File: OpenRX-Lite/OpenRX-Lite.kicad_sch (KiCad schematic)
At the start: 0 parts

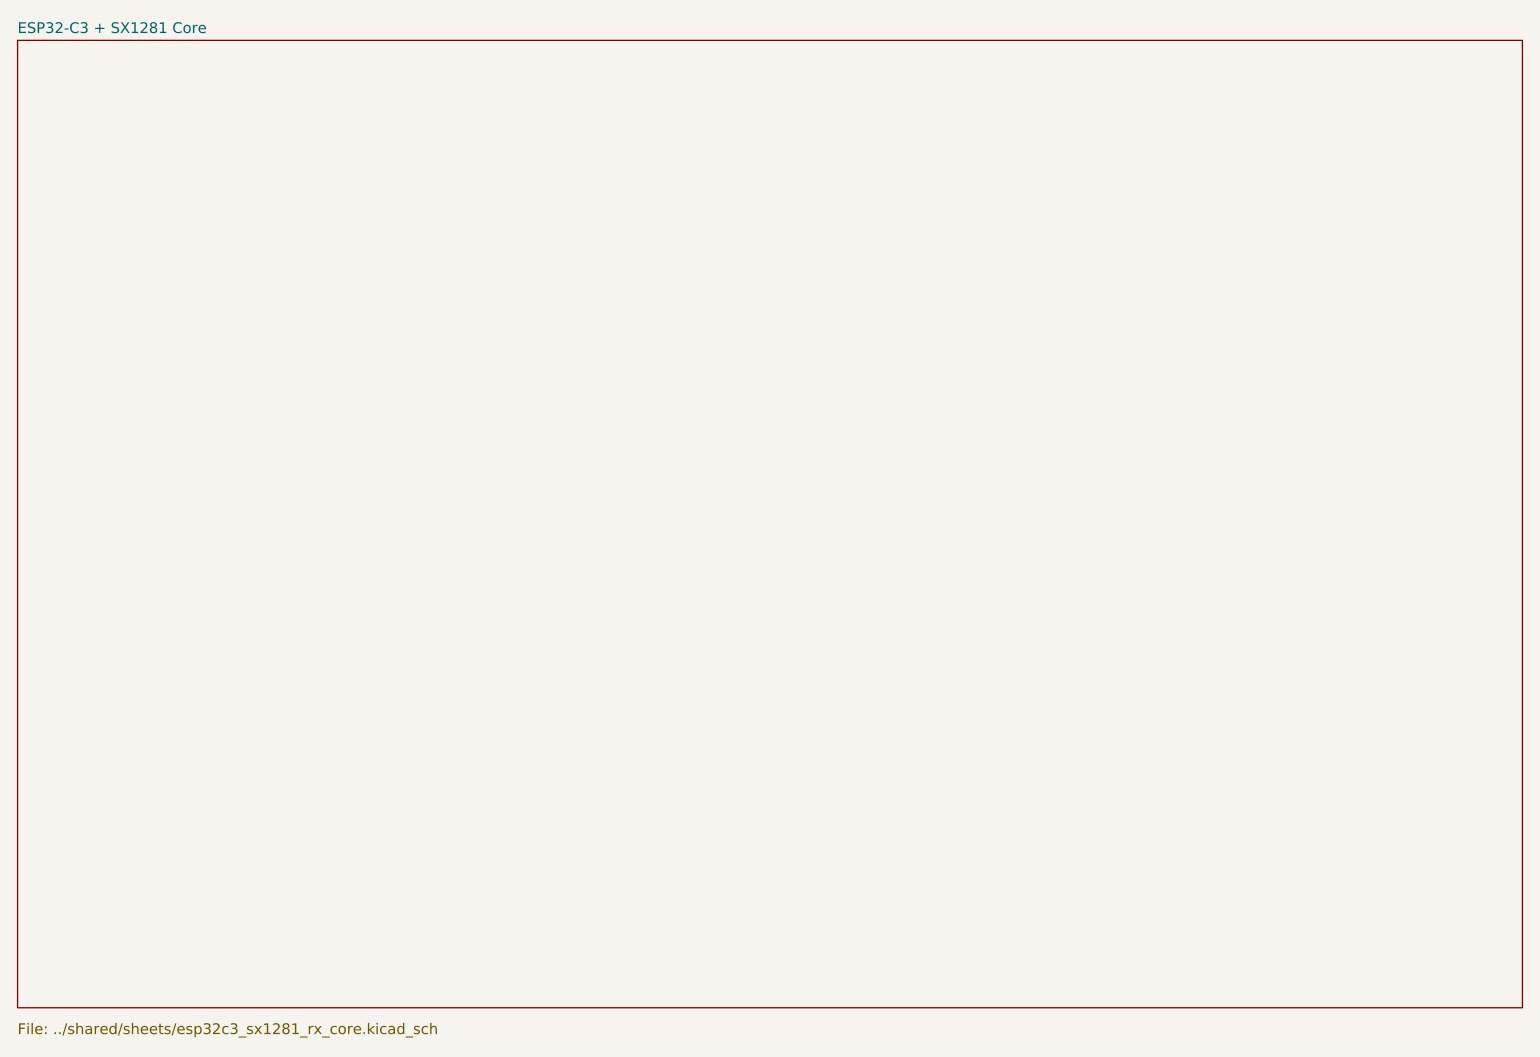
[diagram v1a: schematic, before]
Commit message: Unify library tables, import RFX2401C, Lite schematic capture
- All 6 projects now share OpenRX-Shared + OpenRX-Lite lib tables
- Import RFX2401C (C19213) into shared library with 3D model path fix
- OpenRX-Lite schematic: 0 ERC errors (captured in KiCad GUI)
- Add .gitignore for .lck and .history files
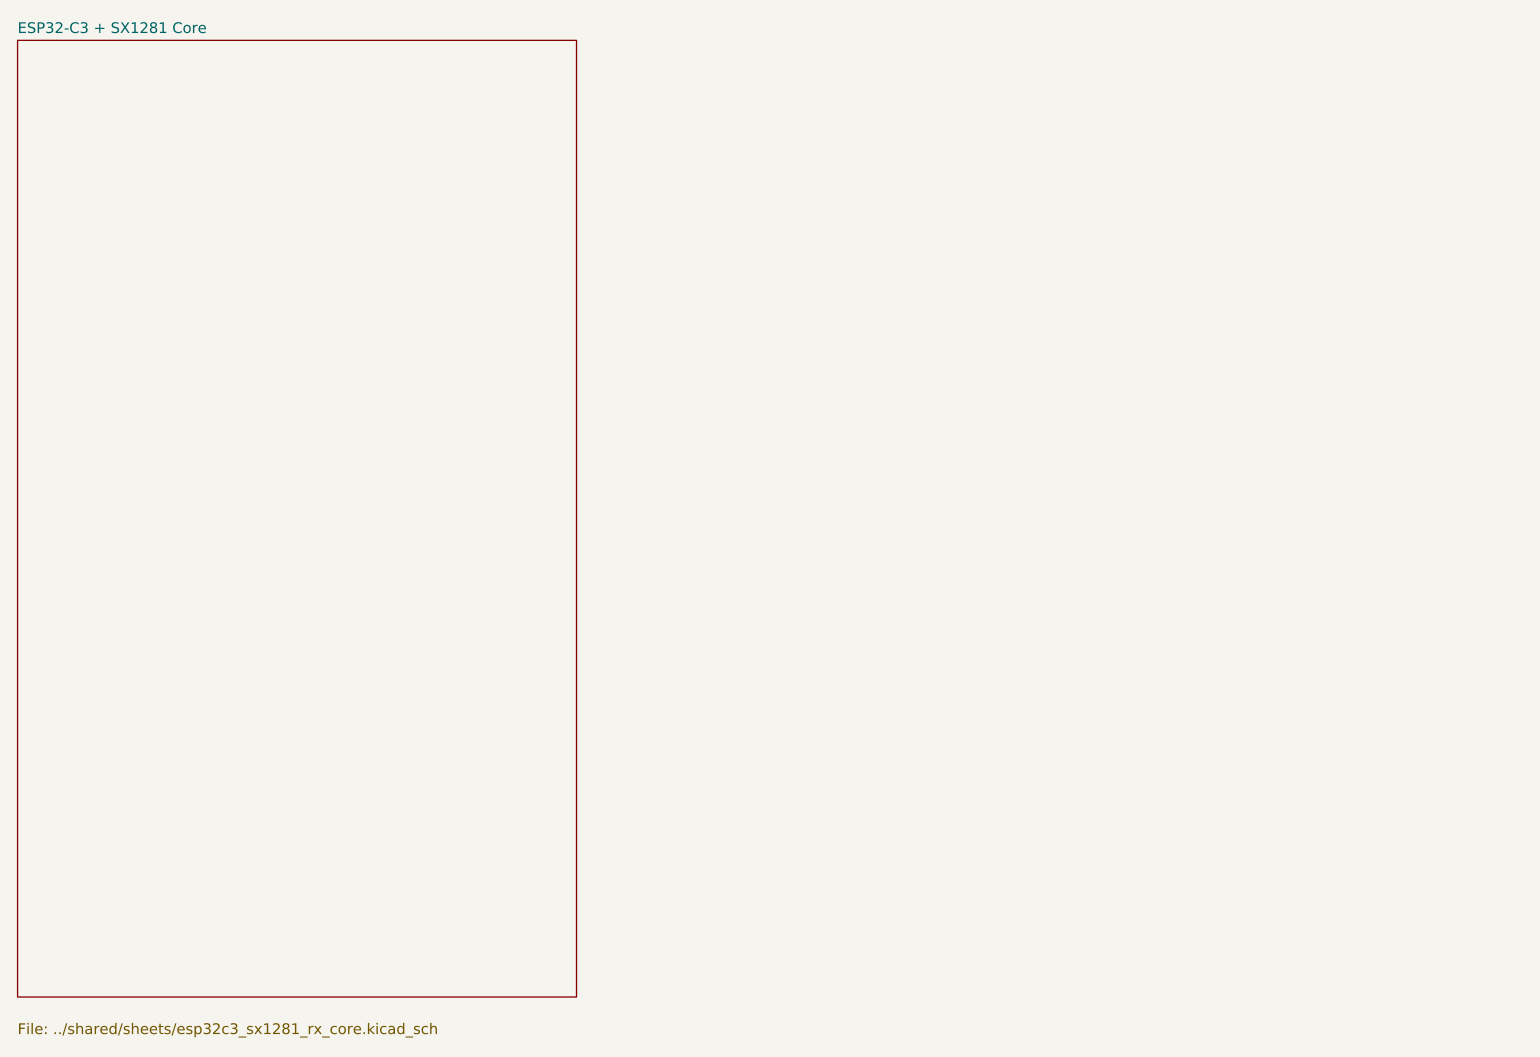
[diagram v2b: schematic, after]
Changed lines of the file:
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@@
 	(sheet
 		(at 25.4 25.4)
-		(size 177.8 114.3)
+		(size 66.04 113.03)
 		(exclude_from_sim no)
 		(in_bom yes)

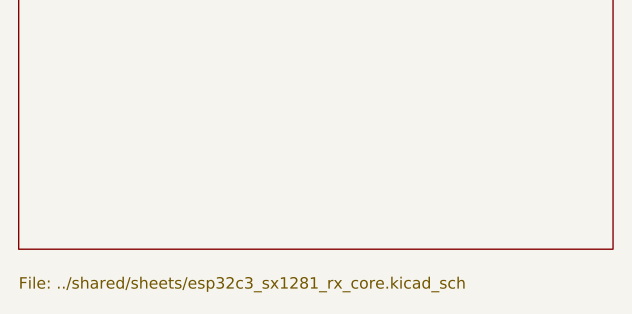
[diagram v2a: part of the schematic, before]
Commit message: Separate Lite and Nano schematics, stop sharing one file
Sharing one .kicad_sch between projects doesn't work - KiCad
overwrites instance data when either project saves.

- Lite: restored pre-Nano schematic as local esp32c3_sx1281_lite.kicad_sch
- Nano: copied current shared sheet as local esp32c3_sx1281_rx_core.kicad_sch
- Each project now has its own schematic file
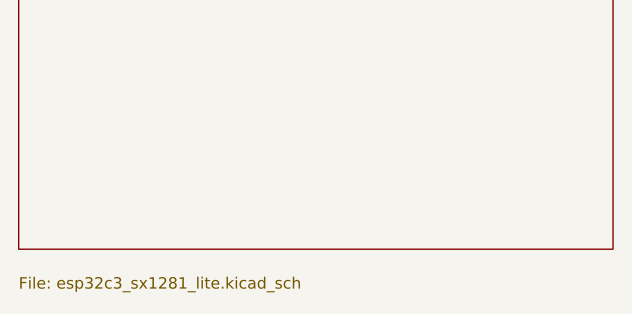
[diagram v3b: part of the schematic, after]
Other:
- sheet ESP32-C3 + SX1281 Core: file ../shared/sheets/esp32c3_sx1281_rx_core.kicad_sch -> esp32c3_sx1281_lite.kicad_sch
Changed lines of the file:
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@@
 			)
 		)
-		(property "Sheetfile" "../shared/sheets/esp32c3_sx1281_rx_core.kicad_sch"
+		(property "Sheetfile" "esp32c3_sx1281_lite.kicad_sch"
 			(at 25.4 141.478 0)
 			(show_name no)
